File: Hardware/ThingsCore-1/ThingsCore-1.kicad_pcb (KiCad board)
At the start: 6 copper layers, 30 x 51 mm, 203 parts, among them IC1 WF200SD, J1 Conn_Coaxial, Q1 Si2371EDS, Q2 Si2371EDS, Q3 2N7002, U10 EMMC04G-M627-A01, U2 K4B4G1646E-BYMA, U3 TLV62569DBV, U4 TLV62569DBV, U5 TLV62569DBV, U6 LAN8742A, U7 STM32MP133DAE7, U8 W25Q256JVEIQ, U9 TF-123B-ARP9H17, Y1 X322516MLB4SI, Y2 Q13FC13500004, Y3 C3SB38.400F09E12, Y4 X322525MOB4SI

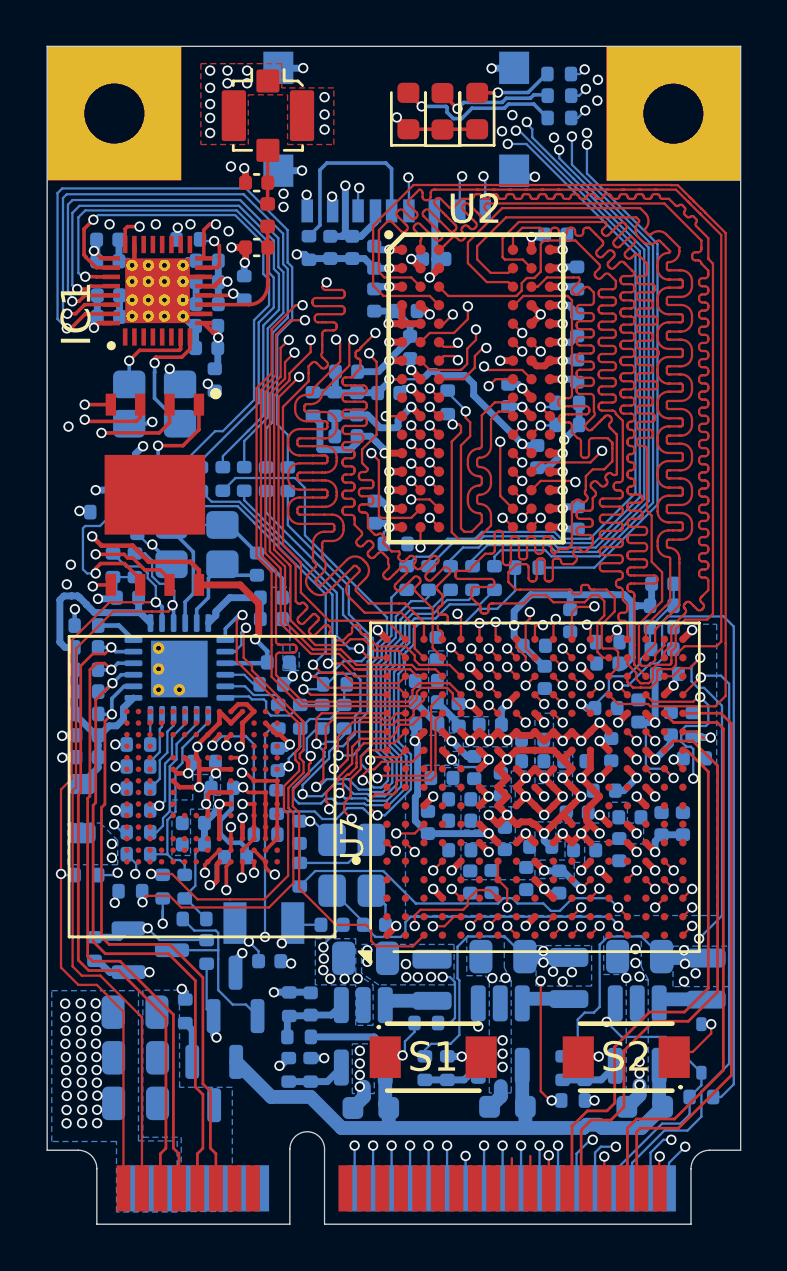
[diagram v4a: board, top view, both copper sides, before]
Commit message: checks left and feedback resistors for switchers
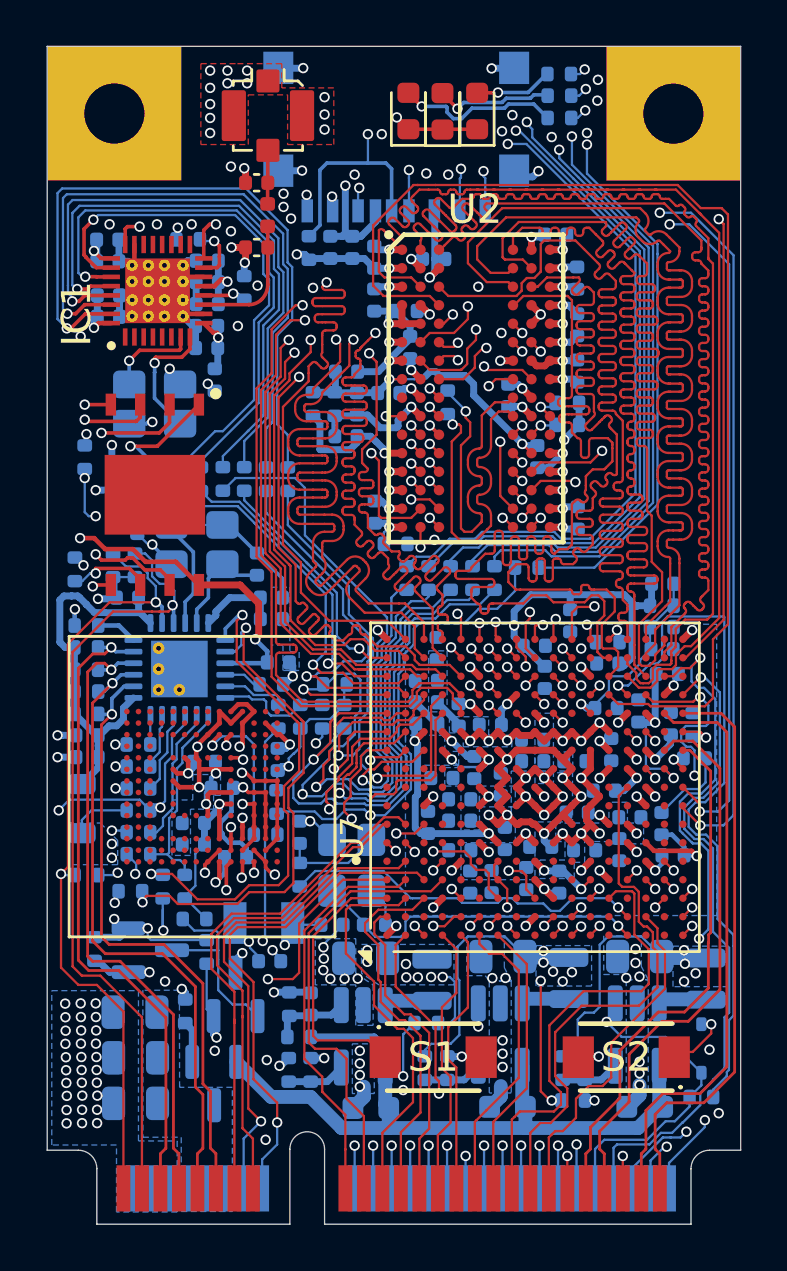
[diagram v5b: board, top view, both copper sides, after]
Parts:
- added R29: 10k, Resistor_SMD:R_0402_1005Metric, B.Cu at (14.0, 30.2)
- moved R23 2.74 mm to (13.6, 35.0), turned to -90 degrees
- moved C45 1.44 mm to (39.5, 47.4), turned to 0 degrees
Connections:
- R26 pad 2: /MEMORY/SD_DET -> SD_DET
- R34 pad 2: /MPU-IO/VDD_LD -> 3V3_VDD
- R54 pad 1: /NETWORKING/ETH_RST -> ETH_RST
- R54 pad 2: GND -> 3V3_VDD
- U1 pad 13: unconnected-(U1-Pad13) -> UART4_RX
- U1 pad 14: unconnected-(U1-Pad14) -> UART8_TX
- U1 pad 15: unconnected-(U1-Pad15) -> I2C1_SDA
- U1 pad 16: unconnected-(U1-Pad16) -> SPI4_MISO
- U1 pad 17: unconnected-(U1-Pad17) -> SPI4_SCK
- U1 pad 19: unconnected-(U1-Pad19) -> SPI4_MOSI
- U1 pad 21: unconnected-(U1-Pad21) -> UART8_CTS
- U1 pad 23: unconnected-(U1-Pad23) -> UART8_RTS
- U1 pad 25: unconnected-(U1-Pad25) -> UART4_TX
- U1 pad 27: unconnected-(U1-Pad27) -> I2C1_SCL
- U1 pad 29: unconnected-(U1-Pad29) -> FDCAN1_RX
- U1 pad 31: unconnected-(U1-Pad31) -> FDCAN1_TX
- U1 pad 33: unconnected-(U1-Pad33) -> UART8_RX
- U1 pad 35: unconnected-(U1-Pad35) -> I2C3_SDA
- U1 pad 37: unconnected-(U1-Pad37) -> USART6_TX
- U1 pad 39: GND -> I2C3_SCL
- U1 pad 41: /MPU-IO/USB2_N -> GND
- U1 pad 42: GND -> 3V3_VDD
- U1 pad 43: /MPU-IO/USB2_P -> /MPU-IO/USB2_N
- U1 pad 44: NRST -> PWR_ONRST
- U1 pad 45: GND -> /MPU-IO/USB2_P
- U1 pad 46: PWR_ONRST -> BOOT0
- U1 pad 47: /MPU-IO/USB1_P -> GND
- U1 pad 48: BOOT0 -> BOOT1
- U1 pad 49: /MPU-IO/USB1_N -> /MPU-IO/USB1_P
- U1 pad 50: BOOT1 -> BOOT2
- U1 pad 51: GND -> /MPU-IO/USB1_N
- U1 pad 52: BOOT2 -> NRST
- U10 pad D4: (no net) -> GND
- U6 pad 15: /NETWORKING/ETH_RST -> ETH_RST
- U7 pad A2: unconnected-(U7D-PA9-PadA2) -> UART4_TX
- U7 pad A3: unconnected-(U7D-PD10-PadA3) -> /MPU-IO/USER_SW
- U7 pad A4: unconnected-(U7D-PB7-PadA4) -> TRX_IRQ
- U7 pad A7: unconnected-(U7E-PE8-PadA7) -> I2C1_SDA
- U7 pad B1: unconnected-(U7D-PD3-PadB1) -> ETH_RST
- U7 pad B3: unconnected-(U7D-PD14-PadB3) -> UART8_CTS
- U7 pad B4: unconnected-(U7E-PE12-PadB4) -> SPI4_SCK
- U7 pad B5: unconnected-(U7E-PE1-PadB5) -> UART8_TX
- U7 pad B7: unconnected-(U7E-PH14-PadB7) -> UART4_RX
- U7 pad C3: unconnected-(U7E-PE14-PadC3) -> UART8_RTS
- U7 pad C4: unconnected-(U7E-PE13-PadC4) -> SPI4_MISO
- U7 pad D1: unconnected-(U7D-PB8-PadD1) -> I2C1_SCL
- U7 pad D4: unconnected-(U7E-PE11-PadD4) -> SPI4_MOSI
- U7 pad E1: unconnected-(U7E-PG9-PadE1) -> FDCAN1_RX
- U7 pad F1: unconnected-(U7E-PG10-PadF1) -> FDCAN1_TX
- U7 pad G1: unconnected-(U7E-PF9-PadG1) -> UART8_RX
- U7 pad J3: unconnected-(U7E-PI2-PadJ3) -> TRX_WUP
- U7 pad N3: unconnected-(U7D-PD7-PadN3) -> I2C3_SDA
- U7 pad P9: unconnected-(U7E-PG14-PadP9) -> USART6_TX
- U7 pad R2: unconnected-(U7E-PH3-PadR2) -> I2C3_SCL
- U7 pad U16: unconnected-(U7E-PI7-PadU16) -> SD_DET
- U7 pad U8: unconnected-(U7D-PC1-PadU8) -> /MPU-IO/USER_LD
- U7 pad U9: unconnected-(U7D-PC2-PadU9) -> /MPU-IO/HB_LD
- U9 pad 9: /MEMORY/SD_DET -> SD_DET
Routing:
- net TRX_WUP: track 1.85 -> 55.4 mm, vias 1 -> 2
- net SD_DET: track 0.00 -> 52.7 mm, vias 0 -> 2
- net TRX_IRQ: track 1.34 -> 49.5 mm, vias 1 -> 2
- net ETH_RST: track 0.00 -> 43.7 mm, vias 0 -> 3
- net /MPU-IO/USER_LD: track 0.67 -> 39.9 mm, vias 1 -> 3
- net /MPU-IO/HB_LD: track 0.75 -> 38.4 mm, vias 1 -> 3
- net USART6_TX: track 0.00 -> 23.0 mm
- net UART4_RX: track 0.00 -> 22.2 mm
- net SPI4_MISO: track 0.00 -> 21.7 mm, vias 0 -> 1
- net UART8_TX: track 0.00 -> 21.1 mm, vias 0 -> 1
- net I2C1_SDA: track 0.00 -> 21.0 mm
- net I2C3_SDA: track 0.00 -> 19.5 mm
- net SPI4_MOSI: track 0.00 -> 19.3 mm
- net /MEMORY/EMMC_~{RST}: track 0.70 -> 18.1 mm, vias 1 -> 3
- net SPI4_SCK: track 0.00 -> 17.2 mm
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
